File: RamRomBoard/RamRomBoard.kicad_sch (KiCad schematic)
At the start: 70 parts, among them J10 ., J13 ., J5 Screw_Terminal_01x02, J6 USB_B_Micro, J7 STM32F401, J8 Dual LED Socket, J9 JTAG, SW1 033TBVSA, U1 74LVC125, U10 74AHC1G14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

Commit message: Readme update
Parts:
- J5: footprint Connector_Phoenix_MC:PhoenixContact_MCV_1,5_2-G-3.81_1x02_P3.81mm_Vertical -> TerminalBlock_RND:TerminalBlock_RND_205-00012_1x02_P5.00mm_Horizontal
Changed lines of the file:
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@@
 			)
 		)
-		(property "Footprint" "Connector_Phoenix_MC:PhoenixContact_MCV_1,5_2-G-3.81_1x02_P3.81mm_Vertical"
+		(property "Footprint" "TerminalBlock_RND:TerminalBlock_RND_205-00012_1x02_P5.00mm_Horizontal"
 			(at 25.4 33.02 0)
 			(effects

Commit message: cpld examples update
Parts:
- U11: value IS61WV102416 -> IS61WV102416FBLL1T2
- U12: value IS61WV10248EDBLL -> IS61WV10248EDBLL-10TL
- U2: footprint Package_TO_SOT_SMD:SOT-89-3_Handsoldering -> Package_TO_SOT_SMD:SOT-223-3_TabPin2
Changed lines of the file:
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@@
 			)
 		)
-		(property "Value" "IS61WV10248EDBLL"
+		(property "Value" "IS61WV10248EDBLL-10TL"
 			(at 262.5441 207.01 0)
 			(effects
@@
 			)
 		)
-		(property "Value" "IS61WV102416"
+		(property "Value" "IS61WV102416FBLL1T2"
 			(at 261.2741 115.57 0)
 			(effects
@@
 			)
 		)
-		(property "Description" "512K x 8 HIGH-SPEED CMOS STATIC RAM, 10ns, TSOP II-44"
+		(property "Description" "512K x 8 HIGH-SPEED CMOS STATIC RAM, 10ns, TSOP II-54"
 			(at 259.08 148.59 0)
 			(effects
@@
 			)
 		)
-		(property "Footprint" "Package_TO_SOT_SMD:SOT-89-3_Handsoldering"
+		(property "Footprint" "Package_TO_SOT_SMD:SOT-223-3_TabPin2"
 			(at 120.65 20.32 0)
 			(effects

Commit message: New XC9572 Example
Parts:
- removed J10, J13: ., Connector_PinHeader_2.00mm:PinHeader_1x01_P2.00mm_Vertical, symbol Connector_Generic:Conn_01x01
- added TP10, TP11, TP12, TP13, TP14, TP15: ., Connector_PinHeader_1.00mm:PinHeader_1x01_P1.00mm_Vertical, symbol Connector:TestPoint
- R1: value 1k -> 560E
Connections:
- net B4 is gone; now on net CLK1#: J7.12 (Pin_12)
- net B14: now also TP14.1
- net B3: now also TP12.1
- net B5: now also TP13.1
- net CLKF: now also U1.8; no longer U1.11
- net CLKF#: now also U1.9; no longer U1.12
- net CLKS: now also U1.11; no longer U1.8
- net CLKS#: now also U1.12; no longer U1.9
- net uA10: now also TP15.1
- net uA4: now also TP11.1
- net CLK1#: now reaches U1.5
- net CLK1: now reaches U1.6
- net SEL4 renamed uA1
- net uA1: now also TP10.1
- net uSCL renamed uSCK
- net uSDA renamed uMOSI
- net ~{uSCL} renamed ~{uSCK}
- no-connect marks 20 -> 21
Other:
- sheet Bus ports: added CLK1, RES0, RES1, RES2, RES3, RES4, RES5, RX0, RX1, TX0, TX1; removed none
- note added: "B4"
- moved on the sheet: C12, U1B, U1C, U1D

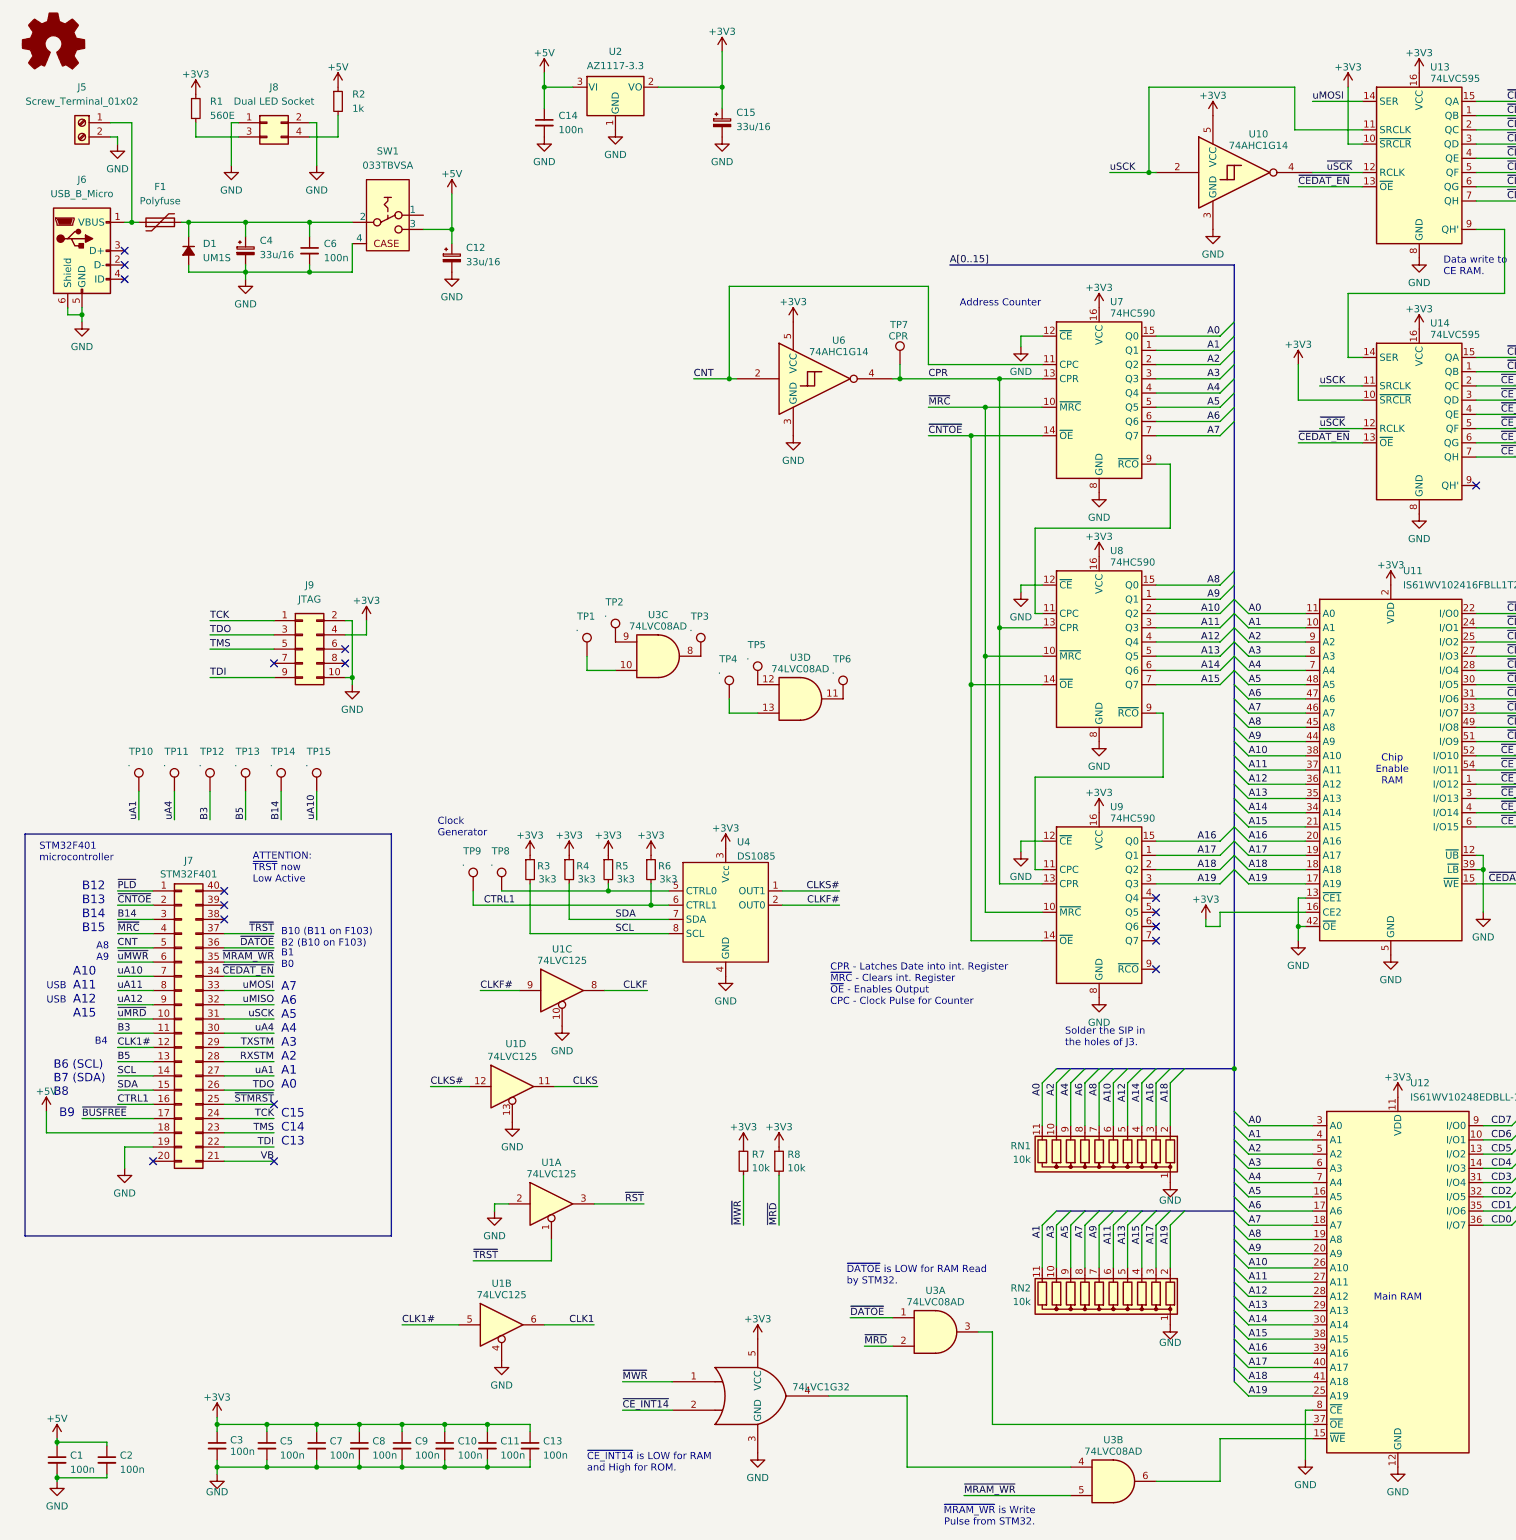
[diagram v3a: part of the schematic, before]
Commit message: Schematics of RAMROM Board updated
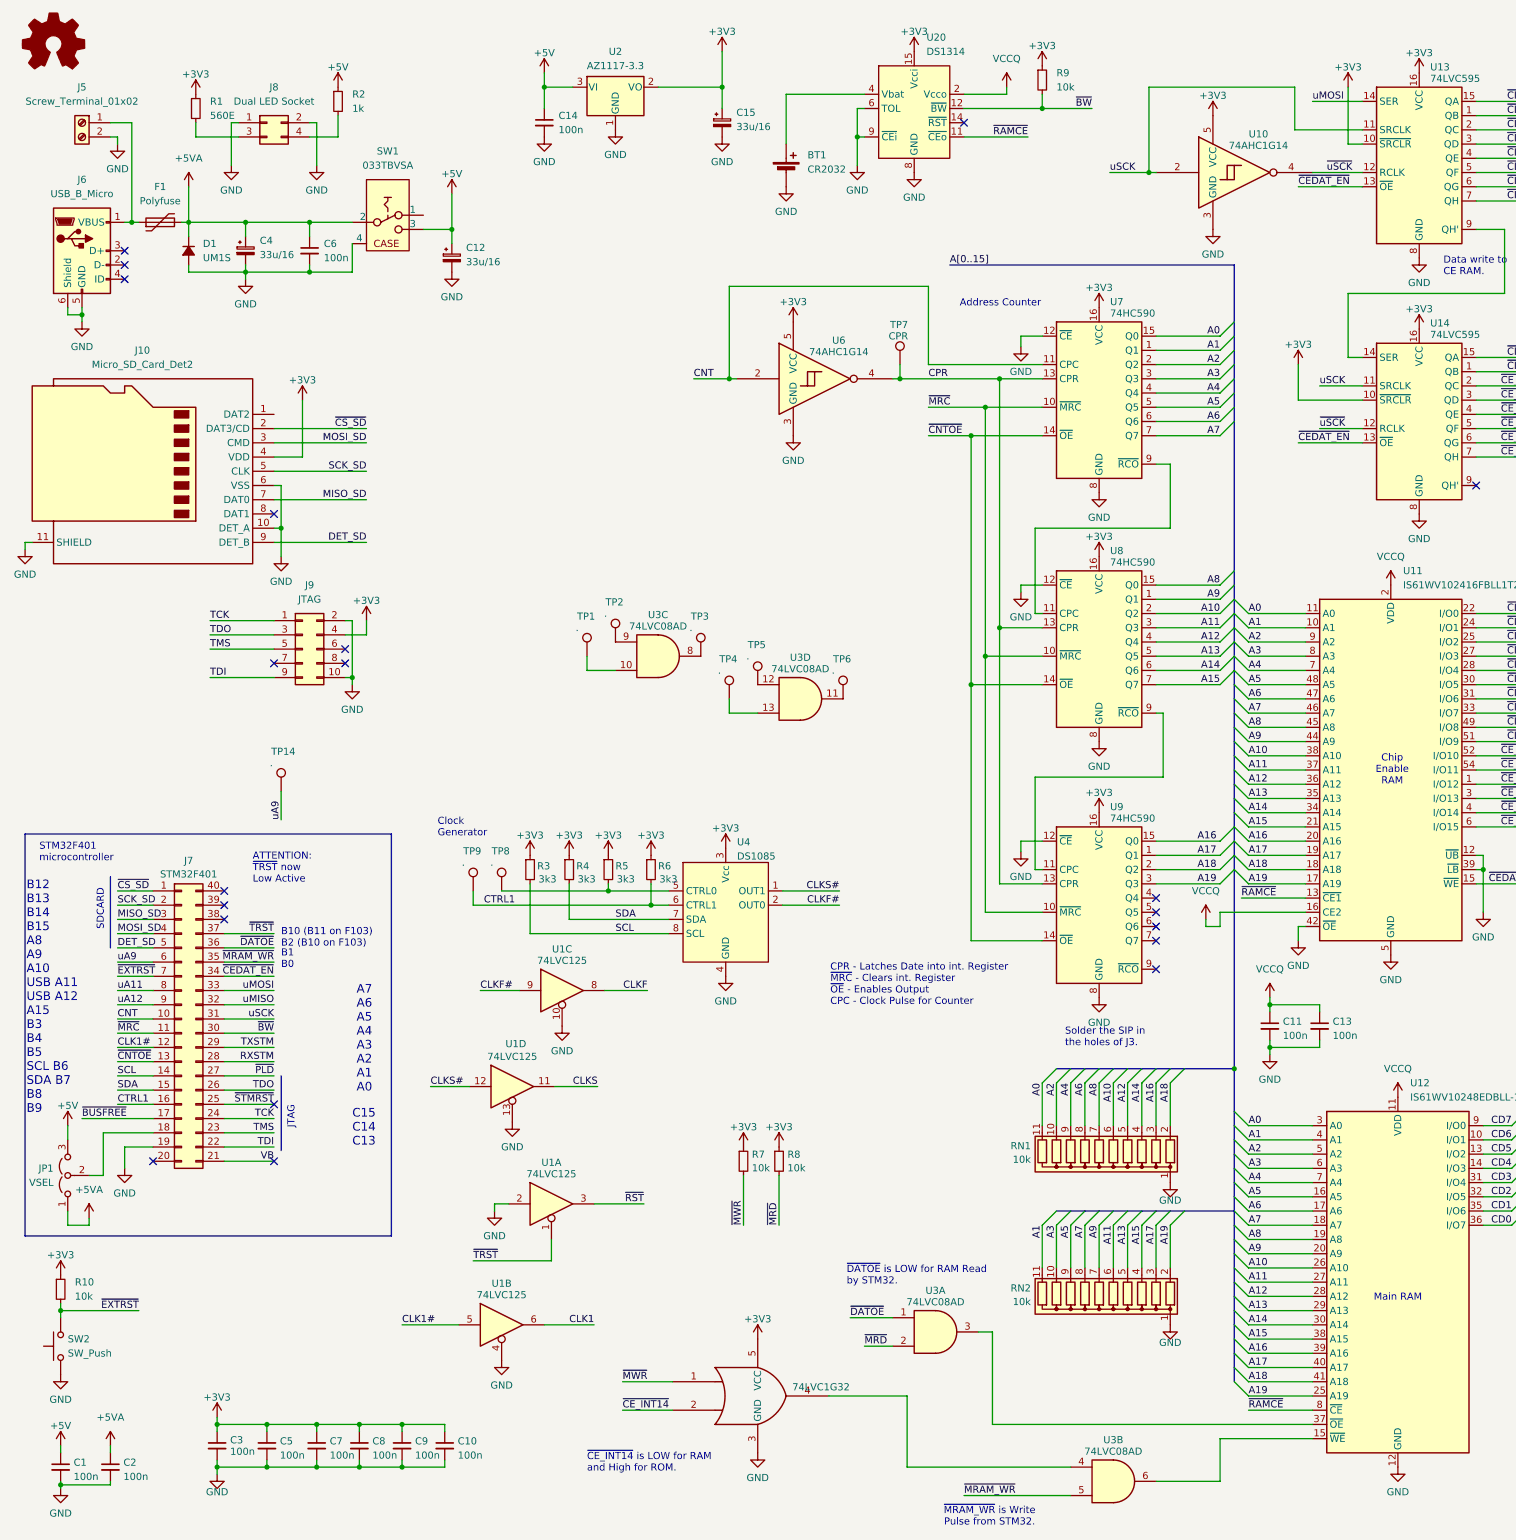
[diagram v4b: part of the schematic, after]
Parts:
- removed TP10, TP11, TP12, TP13, TP15: ., Connector_PinHeader_1.00mm:PinHeader_1x01_P1.00mm_Vertical, symbol Connector:TestPoint
- added BT1: CR2032, my_own:Battery_CR2032_Horizontal_ThreeHoles, symbol Device:Battery_Cell
- added J10: Micro_SD_Card_Det2, Connector_Card:microSD_HC_Hirose_DM3D-SF, symbol Connector:Micro_SD_Card_Det2
- added JP1: VSEL, Connector_PinHeader_2.54mm:PinHeader_1x03_P2.54mm_Vertical, symbol Jumper:Jumper_3_Open
- added R10, R9: 10k, Resistor_SMD:R_1206_3216Metric, symbol Device:R_Small
- added SW2: SW_Push, Button_Switch_THT:SW_Tactile_SPST_Angled_PTS645Vx31-2LFS, symbol Switch:SW_Push
- added U20: DS1314, Package_SO:SOIC-16_3.9x9.9mm_P1.27mm, symbol my_ics_new:DS1314
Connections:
- net B3 is gone; now on net ~{MRC}: J7.11 (Pin_11)
- net B5 is gone; now on net ~{CNTOE}: J7.13 (Pin_13)
- net uA1 is gone; now on net ~{PLD}: J7.27 (Pin_27)
- net ~{uMRD} is gone; now on net CNT: J7.10 (Pin_10)
- net +3V3: now also J10.4 (VDD), R10.1, R9.1, U20.15 (Vcci); no longer C11.1, C13.1, U11.14 (VDD), U11.16 (CE2), U11.2 (VDD), U11.23 (VDD), U11.29 (VDD), U11.50 (VDD), U12.11 (VDD), U12.33 (VDD)
- net +5V: now also JP1.3 (B); no longer C2.1, J7.18 (Pin_18)
- net CNT: no longer J7.5 (Pin_5)
- net GND: now also BT1.2 (-), J10.10 (DET_A), J10.11 (SHIELD), J10.6 (VSS), SW2.1, U20.6 (TOL), U20.8 (GND), U20.9 (~{CEi}); no longer U11.13 (~{CE1}), U12.8 (~{CE})
- net ~{CNTOE}: no longer J7.2 (Pin_2)
- net ~{MRC}: no longer J7.4 (Pin_4)
- net ~{PLD}: no longer J7.1 (Pin_1)
- net +5VA: now reaches C4.1, C6.1, D1.1 (K), F1.2, SW1.2
- net +5VA: now also C2.1, JP1.1 (A)
- net B14 renamed MISO_SD
- net MISO_SD: now also J10.7 (DAT0); no longer TP14.1
- net uA10 renamed ~{EXTRST}
- net ~{EXTRST}: now also R10.2, SW2.2
- net uA4 renamed ~{BW}
- net ~{BW}: now also R9.2, U20.12 (~{BW})
- net ~{uMWR} renamed uA9
- net uA9: now also TP14.1
- new net: BT1.1 (+), U20.4 (Vbat)
- new net: J7.18 (Pin_18), JP1.2 (C)
- new net DET_SD: J10.9 (DET_B), J7.5 (Pin_5)
- new net MOSI_SD: J10.3 (CMD), J7.4 (Pin_4)
- new net SCK_SD: J10.5 (CLK), J7.2 (Pin_2)
- new net VCCQ: C11.1, C13.1, U11.14 (VDD), U11.16 (CE2), U11.2 (VDD), U11.23 (VDD), U11.29 (VDD), U11.50 (VDD), U12.11 (VDD), U12.33 (VDD), U20.2 (Vcco)
- new net ~{CS_SD}: J10.2 (DAT3/CD), J7.1 (Pin_1)
- new net ~{RAMCE}: U11.13 (~{CE1}), U12.8 (~{CE}), U20.11 (~{CEo})
- no-connect marks 21 -> 23
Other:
- note added: "B12 B13 B14 B15 A8 A9 A10 USB A11 USB A12 A15 B3 B4 B5 SCL B6 SDA B7 B8 B9"
- note added: "JTAG"
- note added: "SDCARD"
- note removed: "A10 A11 A12 A15"
- note removed: "A8 A9"
- note removed: "B12 B13 B14 B15"
- note removed: "B4"
- note removed: "B6 (SCL) B7 (SDA) B8"
- note removed: "B9"
- note removed: "USB"
- moved on the sheet: C1, C11, C13, C2

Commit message: Diodes on Databus added, DS1314 different footprint
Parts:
- removed U20: DS1314, Package_SO:SOIC-16_3.9x9.9mm_P1.27mm, symbol my_ics_new:DS1314
- added JP2: MODE1, Jumper:SolderJumper-3_P1.3mm_Bridged12_RoundedPad1.0x1.5mm, symbol Jumper:SolderJumper_3_Bridged12
- added JP3: MODE2, Jumper:SolderJumper-2_P1.3mm_Open_RoundedPad1.0x1.5mm, symbol Jumper:SolderJumper_2_Open
- added TP10: ., Connector_PinHeader_1.00mm:PinHeader_1x01_P1.00mm_Vertical, symbol Connector:TestPoint
- added U20: DS1314, Package_SO:SOIC-8_3.9x4.9mm_P1.27mm, symbol my_ics_new:DS1314_SOIC8
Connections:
- net +3V3: now also U20.8 (VCCi)
- net GND: now also JP3.1 (A), U20. (GND), U20.3 (TOL)
- net VCCQ: now also U20.1 (VCCo)
- net ~{BW}: now also JP2.2 (C), TP10.1
- net ~{RAMCE}: now also U20.6 (~{CEo})
- net at BT1.1 (+): now also U20.2 (Vbat)
- new net: JP2.1 (A), JP3.2 (B), U20.5 (~{CEi})
- new net: JP2.3 (B), U20.7 (~{BW})
- no-connect marks 23 -> 22
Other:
- note added: "~{BW} can either be Battery Warning or RAM Chip Enable. See JP2 and JP3."
- moved on the sheet: BT1, R9

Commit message: many new boards
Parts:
- added JP4: ~{CE_INT14} / ~{CE_EXT14}, Jumper:SolderJumper-3_P1.3mm_Bridged12_RoundedPad1.0x1.5mm, symbol Jumper:SolderJumper_3_Bridged12
- added JP5: RD_Ovr, Jumper:SolderJumper-2_P1.3mm_Open_RoundedPad1.0x1.5mm, symbol Jumper:SolderJumper_2_Open
- added JP6: U3_Ovr, Jumper:SolderJumper-2_P1.3mm_Open_RoundedPad1.0x1.5mm, symbol Jumper:SolderJumper_2_Open
- added JP7: WR_Ovr, Jumper:SolderJumper-2_P1.3mm_Open_RoundedPad1.0x1.5mm, symbol Jumper:SolderJumper_2_Open
- added TP11: ~{CEin}, Connector_PinHeader_1.00mm:PinHeader_1x01_P1.00mm_Vertical, symbol Connector:TestPoint
- JP2: value MODE1 -> ~{CEi} or ~{BW}
- JP3: value MODE2 -> ~{CEi} to GND
- TP10: value . -> ~{BW}
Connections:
- net GND: now also U20.4 (GND); no longer U20. (GND)
- net ~{CE_EXT14}: now also JP4.3 (B)
- net ~{CE_INT14}: now also JP4.1 (A); no longer U5.2
- net ~{MRD}: now also JP5.2 (B)
- net ~{MWR}: now also JP7.2 (B)
- net at U12.37 (~{OE}), U3.3: now also JP5.1 (A)
- net at U12.15 (~{WE}), U3.6: now also JP6.1 (A)
- net at JP2.1 (A), JP3.2 (B), U20.5 (~{CEi}): now also TP11.1
- net at U3.4, U5.4: now also JP6.2 (B), JP7.1 (A)
- net uA9 renamed ~{STM32BUS}
- new net: JP4.2 (C), U5.2
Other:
- sheet Bus ports: added ~{STM32BUS}; removed RES0
- note added: "When using this Board without STM32 and without Chipselect RAM do NOT populate any ICs except: U12, U19 (maybe U20) and close JP5, JP6, JP7."
- note added: "~{CE_INT14} is LOW for RAM and High for ROM (acts as writeprotect)."
- note removed: "~{CE_INT14} is LOW for RAM and High for ROM."
- moved on the sheet: H1, H2, H3, H4, RN3, RN4, TP14
